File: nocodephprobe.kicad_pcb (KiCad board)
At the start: 2 copper layers, 185.7 x 88.6 mm, 31 parts, among them J1 RF1-01 BNC, J2 10K, Q1 2N7002, U1 LMV358a, U2 ICL7106CPL, U3 MCP1501-10xCH, U4 VI-302-DP-RC-S

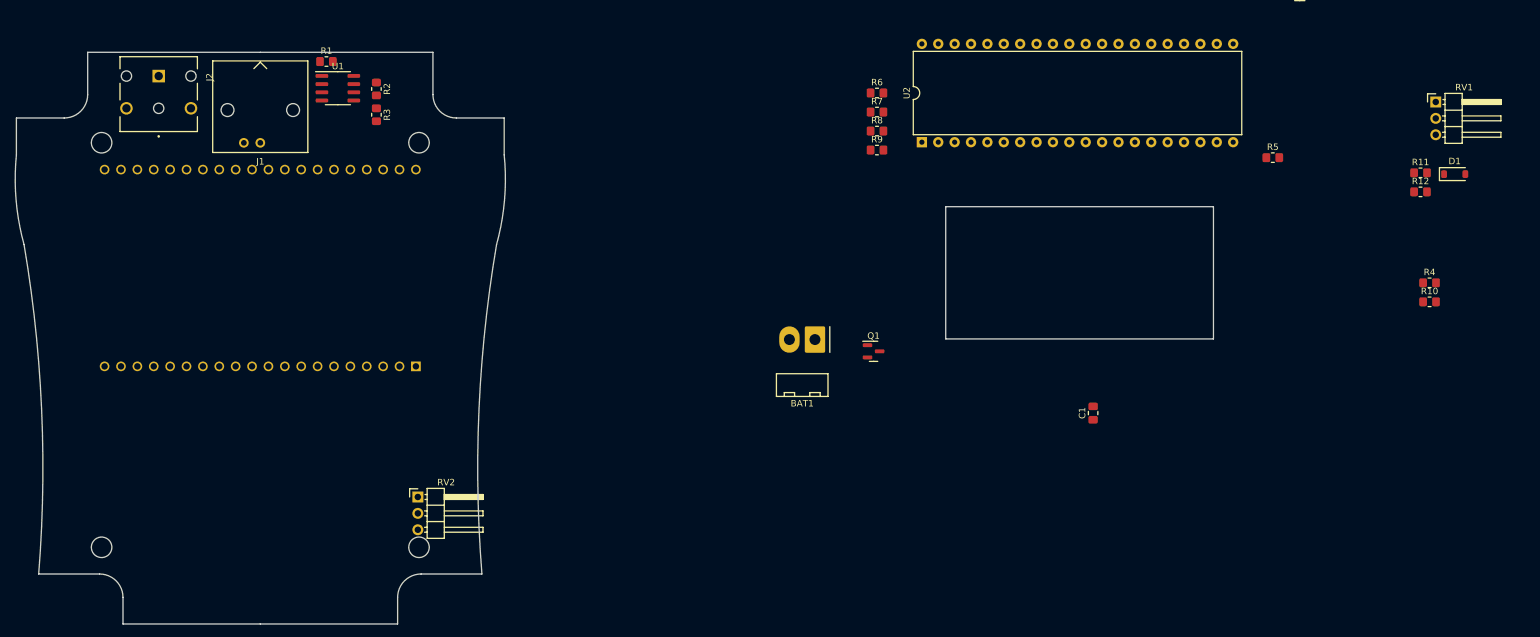
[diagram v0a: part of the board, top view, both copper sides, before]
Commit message: Fix PCB bosses on board outline!
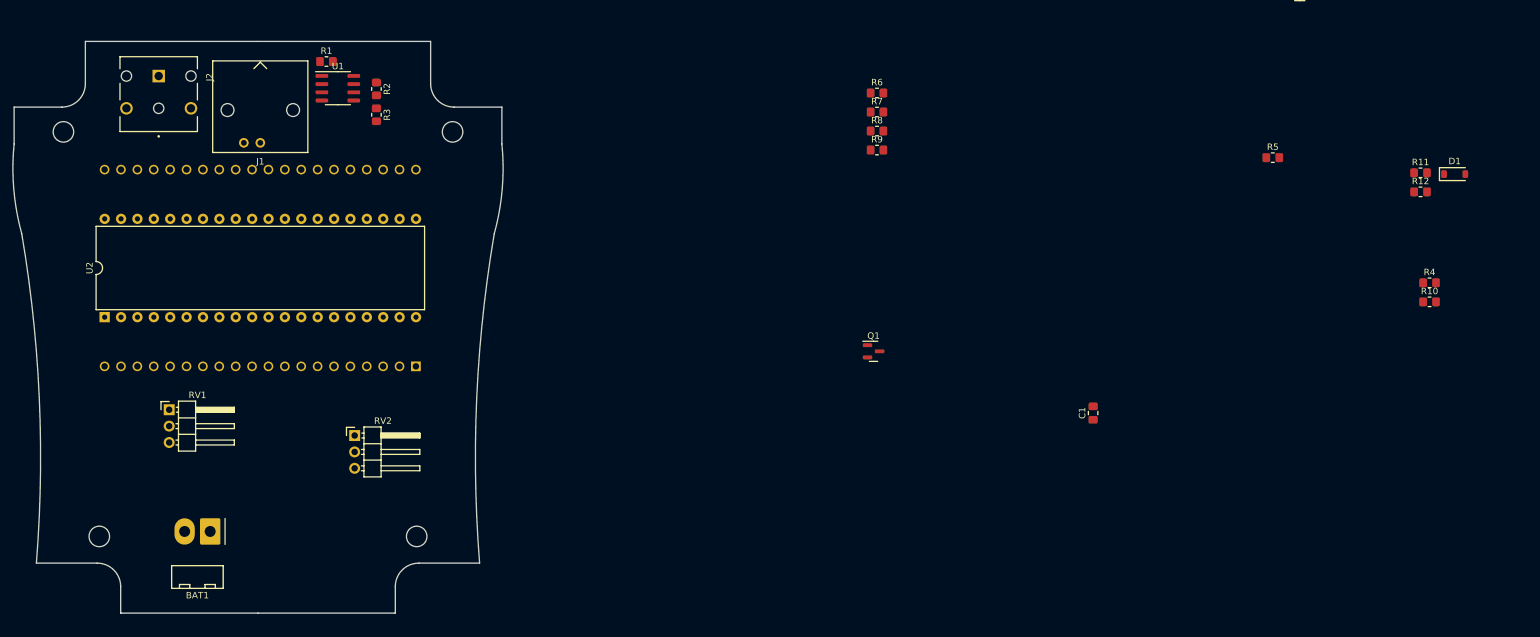
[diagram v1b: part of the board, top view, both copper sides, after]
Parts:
- moved RV1 202.0 mm to (78.9, 110.2)
- moved U2 129.5 mm to (68.9, 95.9)
- moved BAT1 98.4 mm to (85.2, 129.1)
- moved RV2 13.7 mm to (107.6, 114.2)
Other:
- board size 185.7 x 88.6 mm -> 76 x 88.6 mm

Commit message: Add cutout for pots to pcb outline
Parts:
- moved C5 191.5 mm to (123.5, 71.8), turned to -90 degrees
- moved BAT1 39.9 mm to (121.8, 113.0), turned to 90 degrees
- moved R2 30.6 mm to (137.9, 46.0)
- moved R3 30.6 mm to (137.9, 50.0)
- moved RV1 20.4 mm to (60.4, 118.7)
- moved RV2 19.0 mm to (123.4, 124.8), turned to 180 degrees
- moved J2 5.15 mm to (72.5, 56.5)
- moved R1 1.75 mm to (103.2, 54.5)
- moved J1 1.06 mm to (92.6, 69.3)
- moved U1 0.25 mm to (105.2, 60.5)
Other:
- board size 76 x 88.6 mm -> 76 x 80.9 mm

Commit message: Initial routing of nets
No DRC errors, but some mess vias and traces.
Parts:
- added C7: 0.1uF, Capacitor_SMD:C_0805_2012Metric_Pad1.18x1.45mm_HandSolder, F.Cu at (159.0, 75.7)
- moved C6 199.4 mm to (121.9, 92.5)
- moved R13 192.9 mm to (124.3, 74.3), turned to 90 degrees
- moved C2 187.1 mm to (128.5, 74.3), turned to -90 degrees
- moved C3 177.6 mm to (141.0, 75.4), turned to 0 degrees
- moved C4 172.5 mm to (149.6, 74.3)
- moved R14 166.2 mm to (152.9, 74.3), turned to -90 degrees
- moved U3 139.6 mm to (129.5, 108.2)
- moved D1 124.2 mm to (158.6, 107.6), turned to -90 degrees
- moved R11 122.4 mm to (155.4, 108.1), turned to 90 degrees
- moved RV1 119.9 mm to (180.1, 126.0), turned to 180 degrees
- moved R12 111.8 mm to (165.6, 108.1), turned to 90 degrees
- moved R5 104.3 mm to (152.4, 108.1), turned to -90 degrees
- moved R4 101.8 mm to (180.6, 130.5), turned to 90 degrees
- moved R10 98.3 mm to (178.7, 116.6), turned to 180 degrees
- moved C1 96.6 mm to (125.6, 108.0), turned to -90 degrees
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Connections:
- C6 pad 2: -VDC -> GND
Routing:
- net +VDC: track 0.00 -> 134.2 mm
- net BP: track 0.00 -> 126.9 mm, vias 0 -> 5
- net Net-(R2-Pad2): track 0.00 -> 105.6 mm, vias 0 -> 2
- net Net-(J2-Pad5): track 0.00 -> 102.4 mm
- net Net-(J1-Ext): track 0.00 -> 89.2 mm, vias 0 -> 2
- net -VDC: track 0.00 -> 86.6 mm, vias 0 -> 5
- net Net-(U1B-+): track 0.00 -> 82.0 mm, vias 0 -> 2
- net /scaled: track 0.00 -> 64.0 mm
- net Net-(U2-A1): track 0.00 -> 57.9 mm, vias 0 -> 2
- net Net-(U2-F1): track 0.00 -> 54.7 mm, vias 0 -> 2
- net Net-(U2-G1): track 0.00 -> 48.2 mm, vias 0 -> 4
- net Voffset: track 0.00 -> 45.1 mm, vias 0 -> 2
- net Vref: track 0.00 -> 42.0 mm
- net Net-(U2-C3): track 0.00 -> 41.9 mm
- net Net-(C4-Pad2): track 0.00 -> 39.6 mm, vias 0 -> 2
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- added copper zone on B.Cu, net GND
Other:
- rule pad_to_mask_clearance: 0 -> 0.038

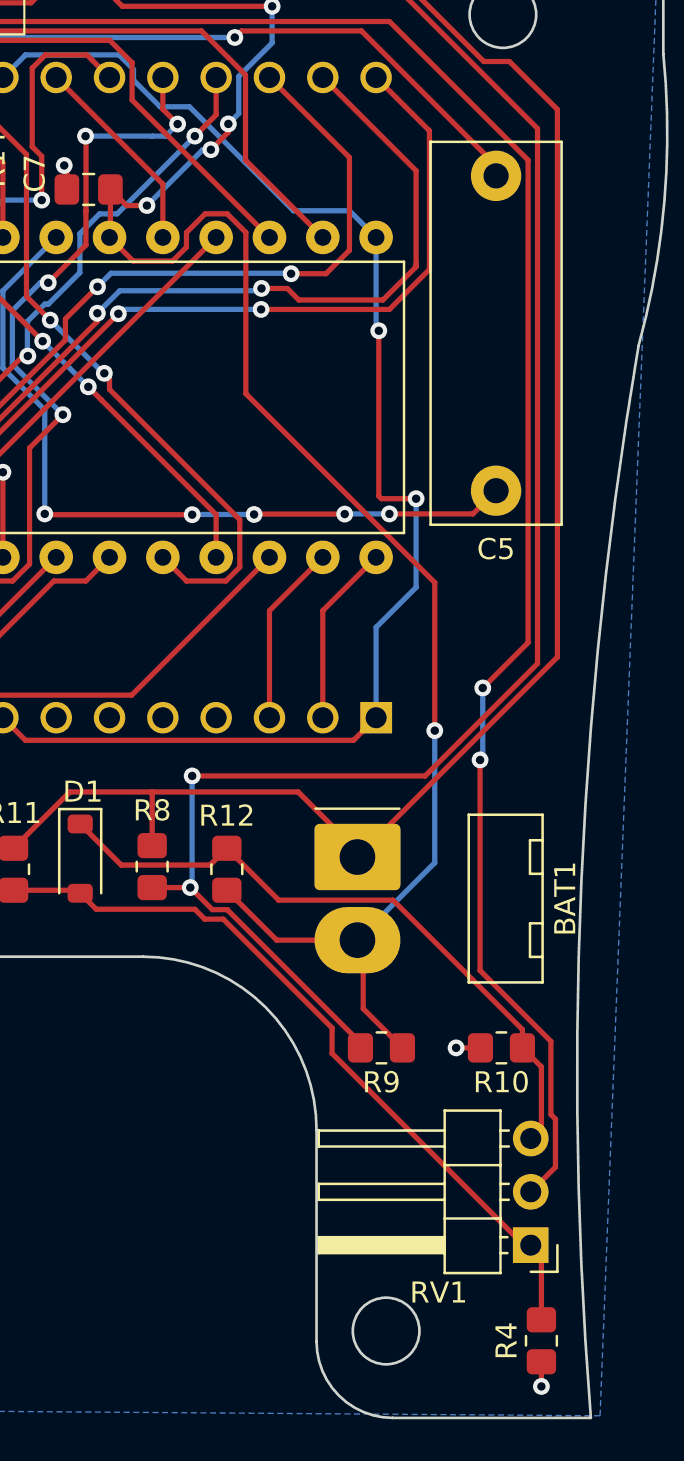
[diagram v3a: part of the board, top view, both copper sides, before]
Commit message: Remove redundant voltage divider
This removes two resistors.
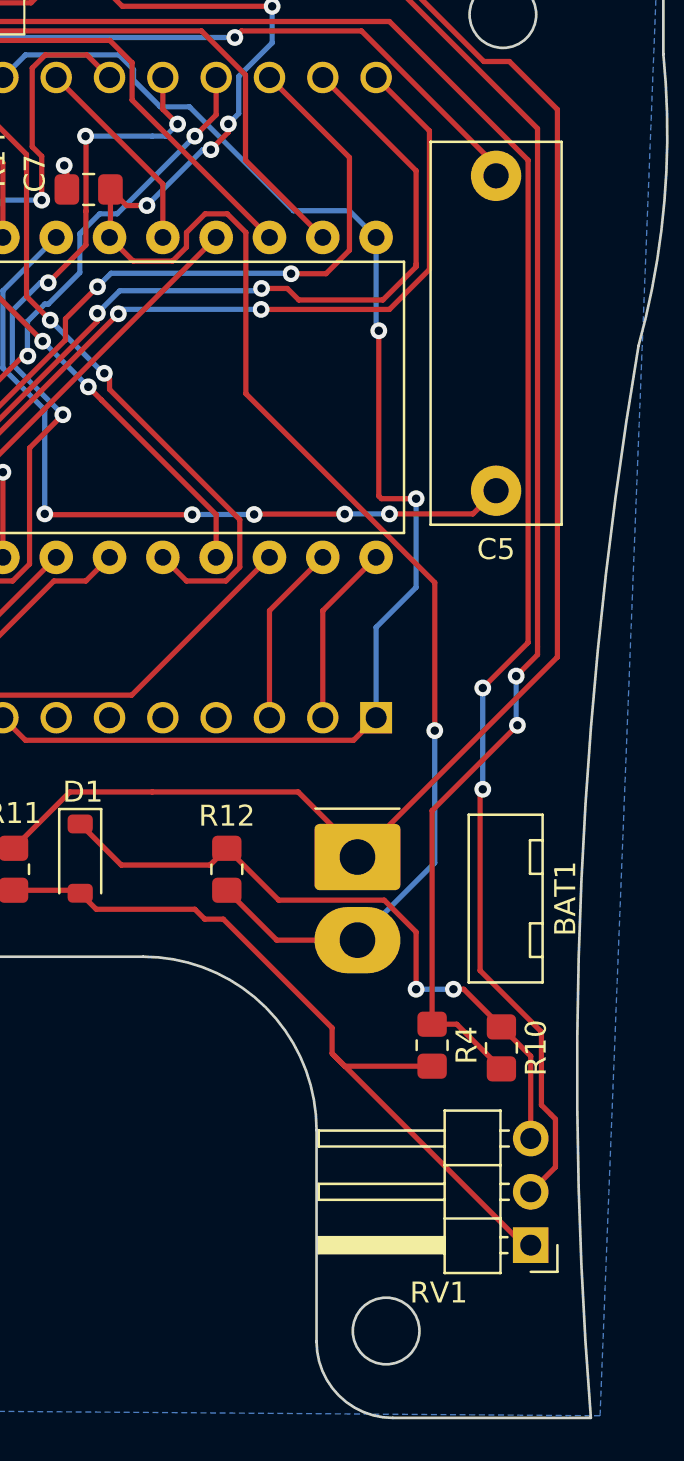
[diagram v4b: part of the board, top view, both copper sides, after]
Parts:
- removed R8, R9: 100K, Resistor_SMD:R_0805_2012Metric_Pad1.20x1.40mm_HandSolder
- moved R4 15.0 mm to (175.4, 116.5), turned to -90 degrees
- turned R10 to -90 degrees
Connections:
- R10 pad 2: GND -> Net-(U1B-+)
- R4 pad 1: GND -> Net-(U1B-+)
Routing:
- net Net-(U1B-+): track 82.0 -> 68.3 mm
- net -VDC: track 86.6 -> 80.6 mm
- net +VDC: track 134.2 -> 131.7 mm
- net GND: track 26.8 -> 24.5 mm, vias 9 -> 7
- net Net-(D1-A): track 36.2 -> 37.3 mm
- net Net-(D1-K): track 31.6 -> 32.2 mm, vias 0 -> 2

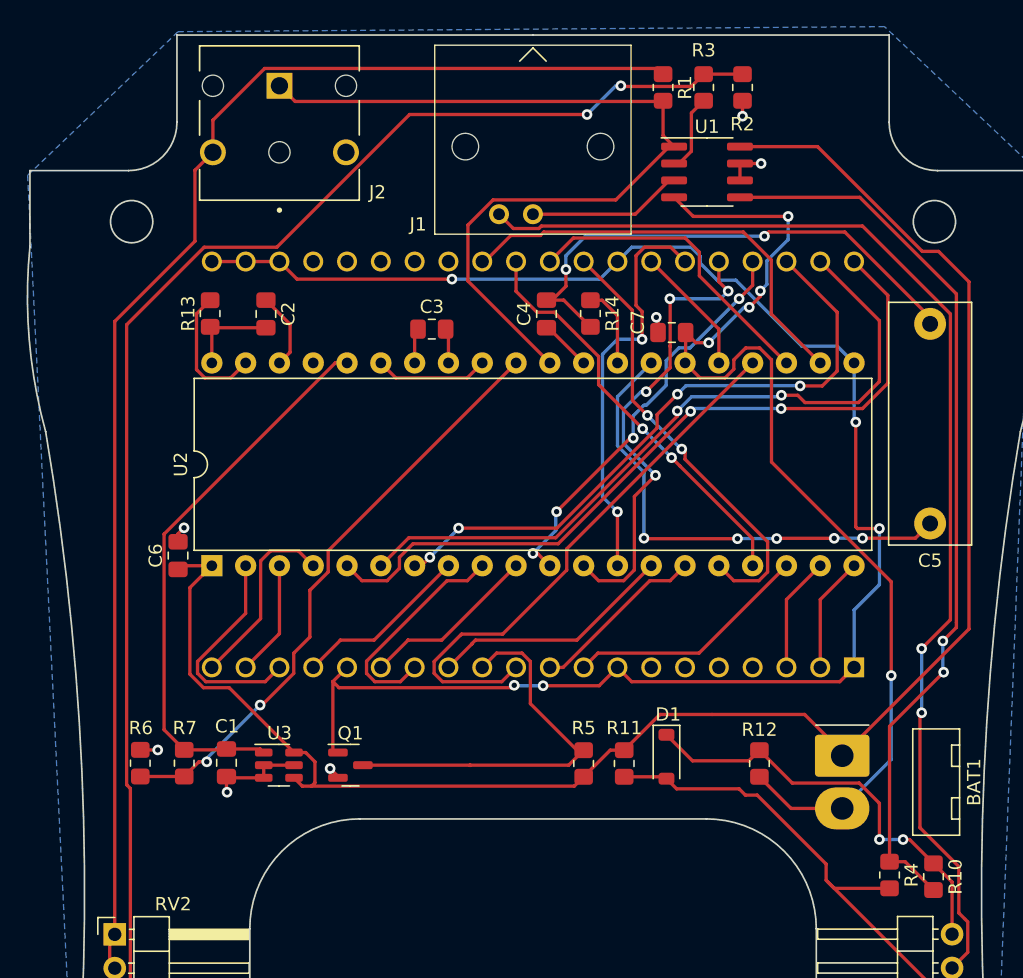
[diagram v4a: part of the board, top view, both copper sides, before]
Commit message: Add revision and github text to silkscreen
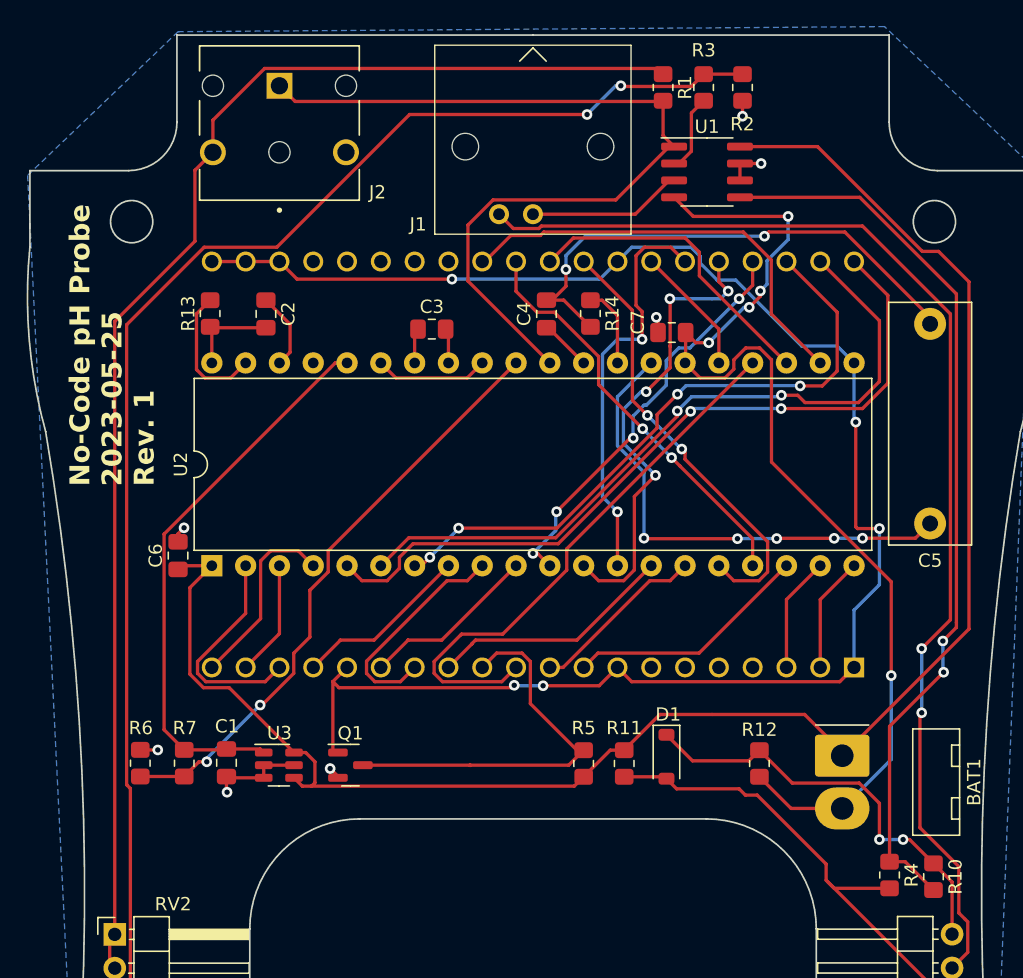
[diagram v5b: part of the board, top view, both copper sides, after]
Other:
- rule pad_to_mask_clearance: 0.038 -> 0
- board text added: "${SITE}"
- board text added: "${TITLE} ${ISSUE_DATE} Rev. ${REVISION}"

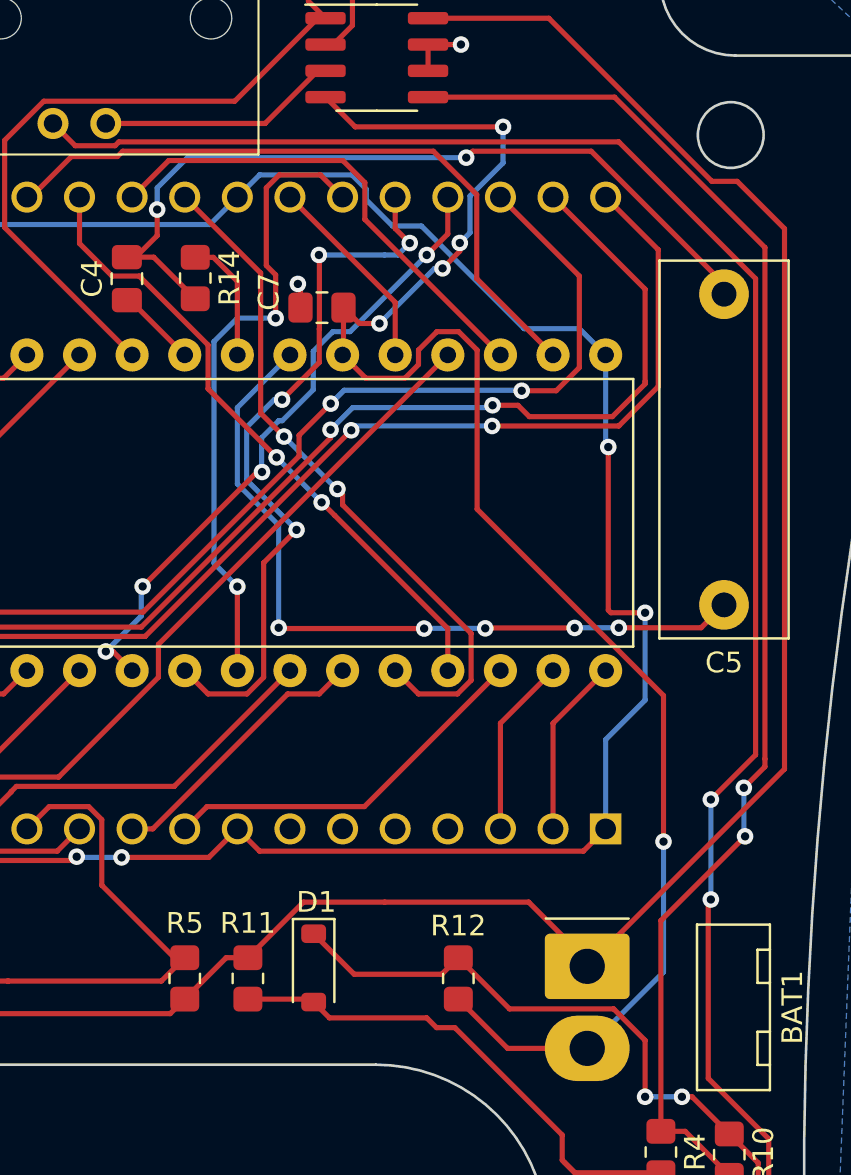
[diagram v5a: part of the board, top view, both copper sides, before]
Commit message: Rework a few traces
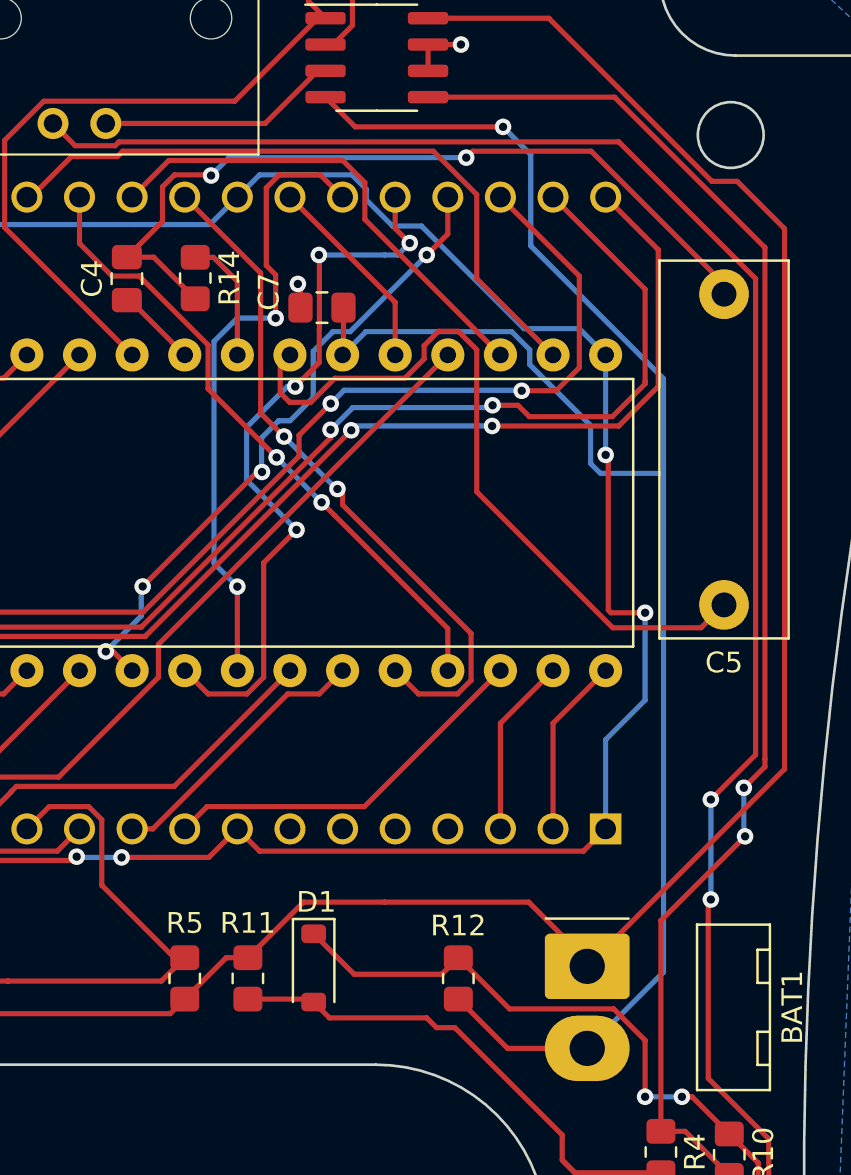
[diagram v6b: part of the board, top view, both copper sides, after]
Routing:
- net -VDC: track 80.6 -> 88.2 mm, vias 5 -> 1
- net Net-(U2-INT): track 37.0 -> 35.8 mm, vias 5 -> 0
